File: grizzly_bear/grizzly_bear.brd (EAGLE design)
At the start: 76.2 x 41.3 mm, 59 parts, among them Q1 N-CHANNEL-MOSFET, Q2 N-CHANNEL-MOSFET, Q3 N-CHANNEL-MOSFET, Q4 N-CHANNEL-MOSFET, Q5 IPD90P03P4L, U1 A4940, U2 ATMEGA32U4-AU, U3 ACS714, U4 UA78L00, Y1 16MHz

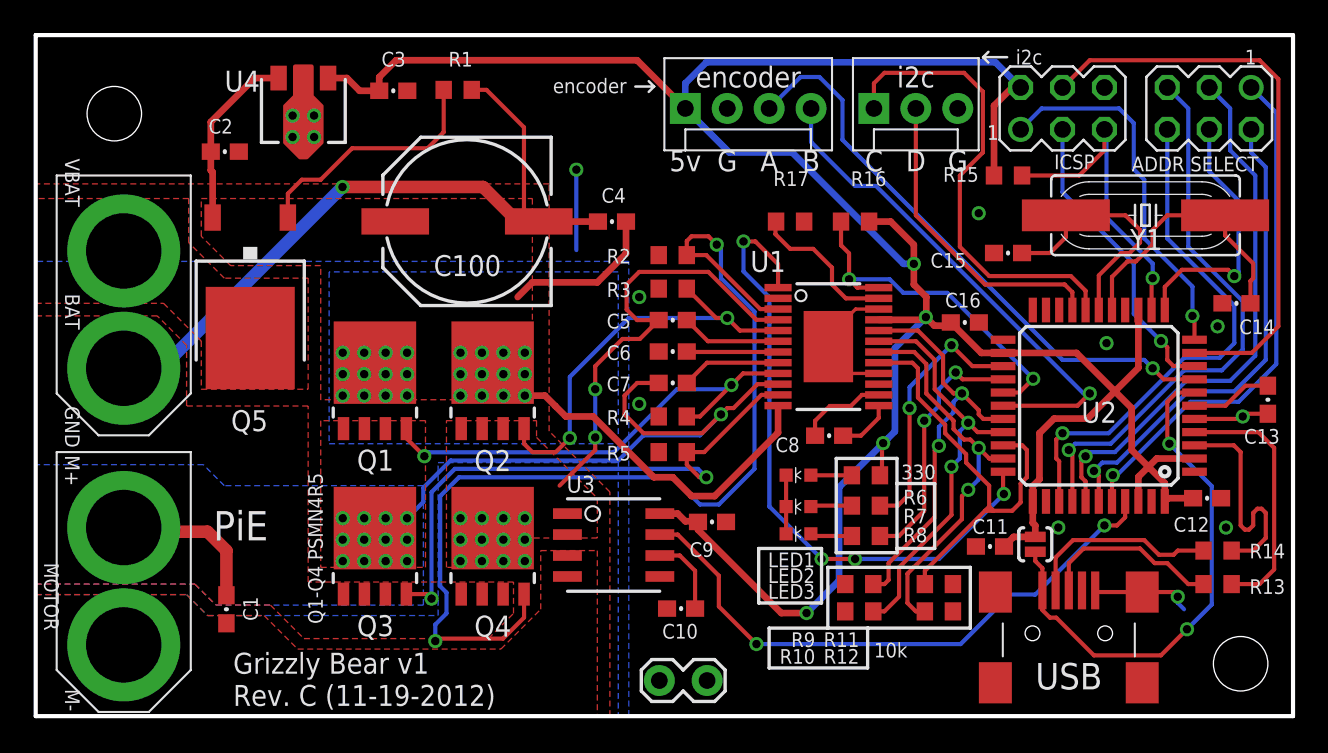
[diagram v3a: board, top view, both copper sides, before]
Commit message: Update Grizzly to Rev. D, mostly fixing grounds
Also fixes:
- Move XT60 connector back closer to edge
- Add GND symbol to pie.lbr
- Change LEDs to new 0805 footprint
- Adjust positions of 18pF caps
- Fix value of Ucap for USB (0.1uF-->1uF)
- Mounting holes on 1/4" grid (was 1/16")
- Use new MTA connector footprint

Change-Id: I2eb2c92b7e9216f9f3d609f47de082e2cb5dc4d4
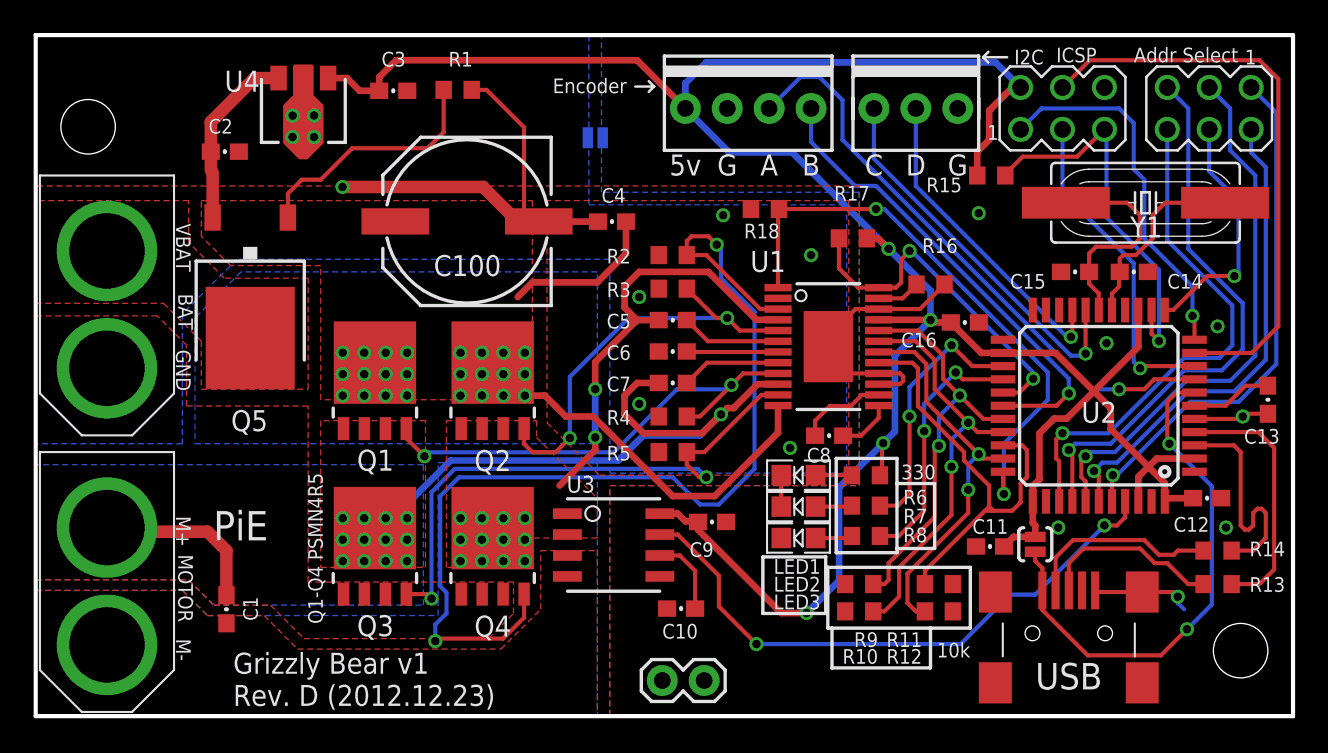
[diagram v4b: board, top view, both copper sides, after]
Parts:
- added R18: 10k, pie:R0603
- added SJ2: SOLDERJUMPERNO, pie:SJ_2S-NO
- C13: value 0.1uF -> 1uF
- JP1: device pie:1X02_LOCK -> pie:1X02
- JP3: device pie:MOLEX-1X4 -> pie:1X04-MTA
- JP4: device pie:MOLEX-1X3 -> pie:1X03-MTA
- LED1: value AMBR -> YEL; device pie:LED-0603 -> pie:LED-0805
- LED2, LED3: device pie:LED-0603 -> pie:LED-0805
- R16: value 10k -> 47k
- R17: value 47k -> 10k
- moved C14 6.51 mm to (66.5, 26.9), turned to 180 degrees
- moved R16 5.95 mm to (54.2, 26.2)
- moved C15 4.22 mm to (63.0, 26.9)
- moved R17 3.94 mm to (49.5, 29.0)
- moved JP3 3.81 mm to (43.2, 36.8)
- moved STANDOFF1 1.77 mm to (3.17, 35.7)
- moved U$18 1.02 mm to (0.25, 32.8)
- moved U$19 1.02 mm to (0.25, 16.0)
- moved R15 1.02 mm to (57.9, 32.8)
- moved STANDOFF2 0.79 mm to (73.0, 3.97)
- moved Y1 0.76 mm to (67.3, 31.1)
- moved LED3 0.25 mm to (46.2, 10.8), turned to 180 degrees
- turned LED1 to 180 degrees
- turned LED2 to 180 degrees
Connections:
- net 5V: now also R17.2; no longer R16.2
- net BATGND: now also C6.2, R16.2, R18.2, R2.2, R3.2, R4.2, R5.2, SJ2.1, U1.15, U1.16, U1.2, U1.22, U1.PAD
- net DRIVER-RESET: now also R18.1
- net FAULT: now also R17.1; no longer R16.1
- net GND: now also SJ2.2; no longer C6.2, R17.2, R2.2, R3.2, R4.2, R5.2, U1.15, U1.16, U1.2, U1.22, U1.PAD
- net RDEAD: now also R16.1; no longer R17.1
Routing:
- net GND: track 27.7 -> 19.0 mm, vias 14 -> 11
- net RDEAD: track 9.24 -> 2.64 mm
- net SCL: track 28.7 -> 23.5 mm, vias 0 -> 1
- net XTAL2: track 17.0 -> 11.9 mm
- net 5V: track 166.4 -> 161.6 mm
- net DRIVER-RESET: track 39.5 -> 35.0 mm, vias 4 -> 2
- net RESET: track 19.1 -> 23.5 mm
- net XTAL1: track 15.4 -> 13.3 mm
- net ENC2: track 30.8 -> 28.8 mm
- net SCK: track 18.4 -> 19.8 mm
- net DIP4: track 15.9 -> 14.8 mm
- net BATGND: track 44.5 -> 43.4 mm, vias 1 -> 6
- net SDA: track 19.0 -> 19.5 mm, vias 0 -> 1
- added copper zone on layer 16, net BATGND
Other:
- board text added: "Addr Select"
- board text added: "Encoder"
- board text added: "I2C"
- board text added: "Rev. D (2012.12.23)"
- board text removed: "ADDR SELECT"
- board text removed: "Rev. C (11-19-2012)"
- board text removed: "encoder"
- board text removed: "i2c"

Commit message: Updated Grizzly to Rev. E, mostly cleaning up sch
Change-Id: Ie27850869d7a5f893dd13d446602863972fe60ee
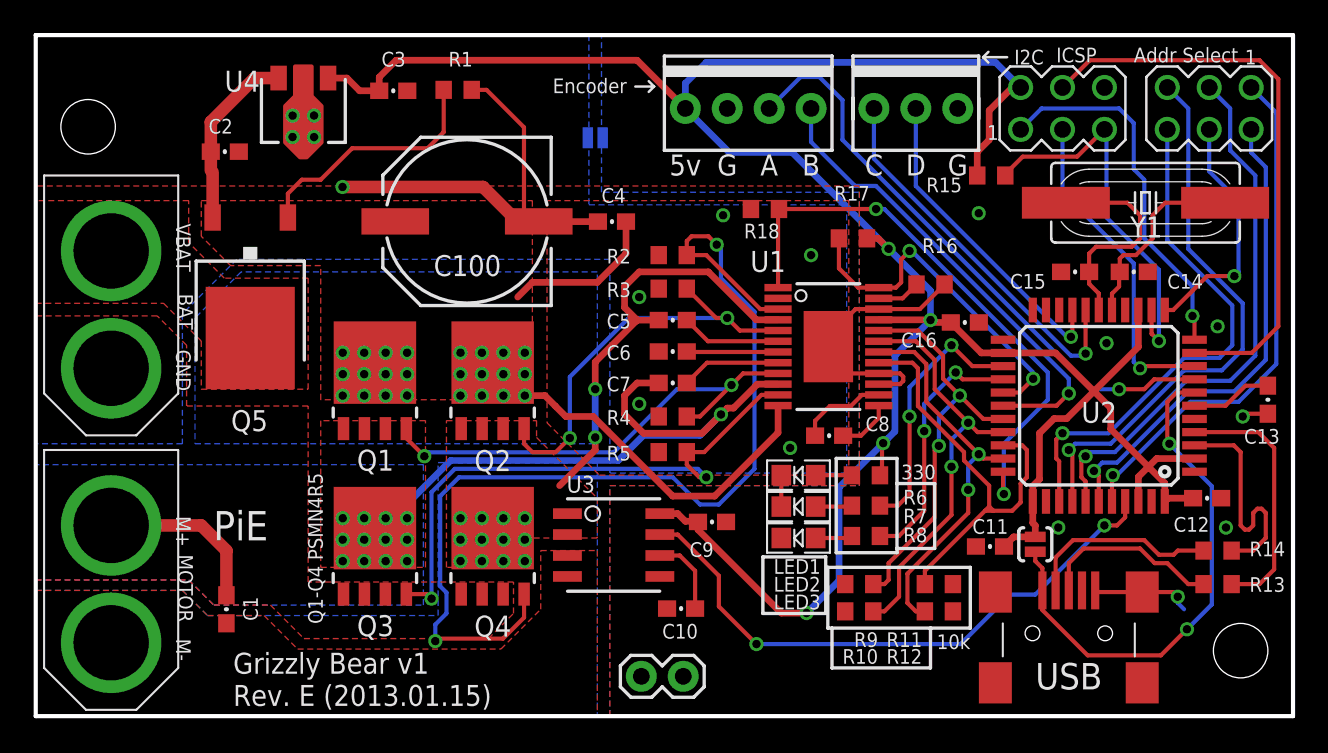
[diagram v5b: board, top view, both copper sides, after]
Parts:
- moved U$18 9.20 mm to (4.57, 24.6)
- moved U$19 9.09 mm to (4.57, 8.00)
- moved JP4 2.54 mm to (53.3, 36.8)
- moved JP1 0.25 mm to (38.0, 2.41)
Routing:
- net GND: track 19.0 -> 16.1 mm
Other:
- board text added: "Rev. E (2013.01.15)"
- board text removed: "Rev. D (2012.12.23)"

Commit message: Update silkscreen, copyright, paste on Grizzly
Change-Id: I853ac7017a0e5a7d6539925bc642fb125ce048da
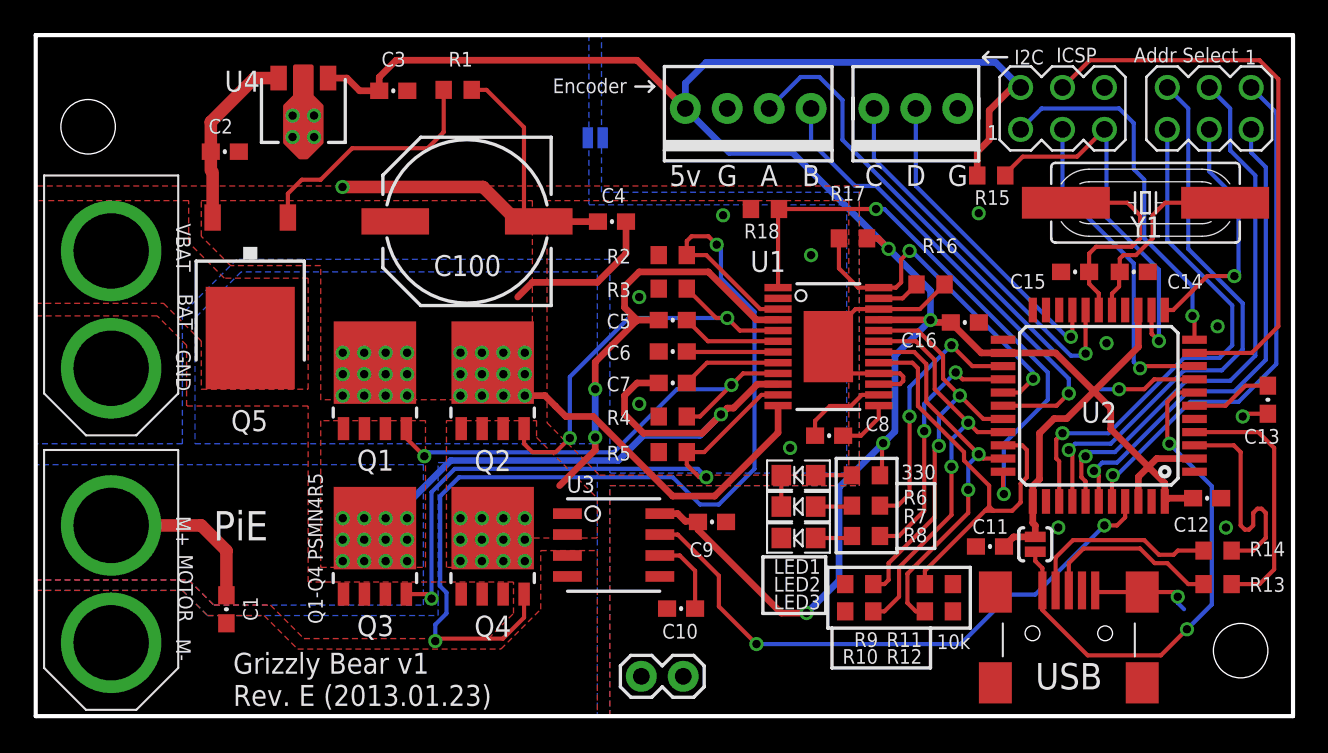
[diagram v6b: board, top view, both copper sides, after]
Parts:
- added U$1: (no value), pie:OSHW-LOGO-L
- turned JP3 to 180 degrees
- turned JP4 to 180 degrees
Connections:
- net 5V: now also JP3.4; no longer JP3.1
- net ENC1: now also JP3.2; no longer JP3.3
- net ENC2: now also JP3.1; no longer JP3.4
- net GND: now also JP3.3, JP4.1; no longer JP3.2, JP4.3
- net SCL: now also JP4.3; no longer JP4.1
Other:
- board text added: "Copyright (c) 2013, Pioneers in Engineering All rights reserved."
- board text added: "Design by: Jay Chenn, Keegan Mann, Robert Ou This design is open source hardware. For more information, visit pioneers.berkeley.edu/opensource"
- board text added: "Rev. E (2013.01.23)"
- board text removed: "Rev. E (2013.01.15)"

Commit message: rev F renamed to grizzly_bear 11/13
solder jumper replaced with large trace to connect ground planes,
copyright info stop mask conflicts resolved
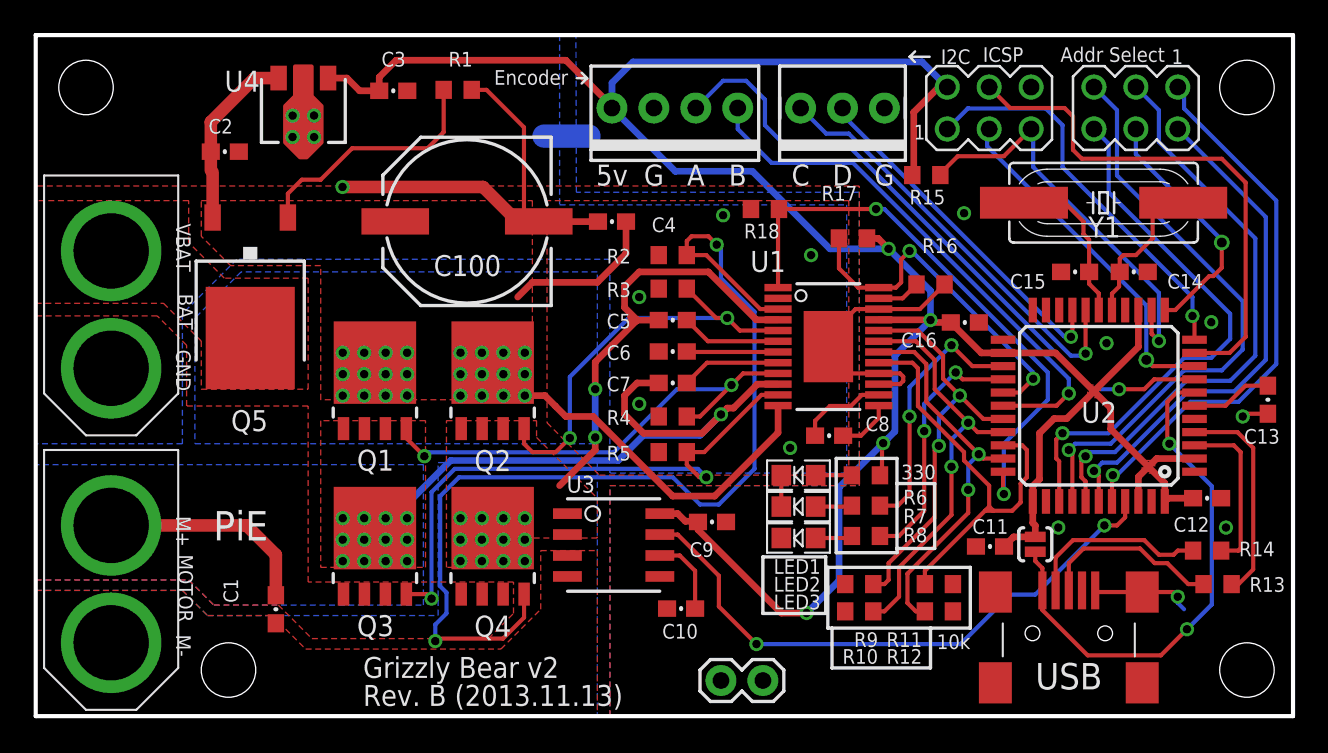
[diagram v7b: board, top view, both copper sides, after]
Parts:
- removed SJ2: SOLDERJUMPERNO, pie:SJ_2S-NO
- added STANDOFF3, STANDOFF4: STAND-OFF, pie:STAND-OFF
- moved JP1 4.83 mm to (42.8, 2.16), turned to 180 degrees
- moved SV1 4.45 mm to (66.7, 36.9)
- moved JP3 4.45 mm to (38.7, 36.9)
- moved JP4 4.45 mm to (48.9, 36.9)
- moved JP6 4.45 mm to (57.8, 36.9)
- moved R15 3.94 mm to (54.0, 32.8)
- moved C1 3.00 mm to (14.6, 6.48)
- moved Y1 2.54 mm to (64.7, 31.1)
- moved STANDOFF1 2.38 mm to (3.05, 38.1)
- moved STANDOFF2 1.23 mm to (73.4, 2.79)
- moved R14 0.64 mm to (71.0, 10.0)
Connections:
- removed net GND: C10.1, C11.1, C12.2, C13.2, C14.1, C15.1, C16.2, C2.2, C3.2, C9.2, JP1.1, JP1.2, JP3.3, JP4.1, JP6.6, LED1.C, LED2.C, LED3.C, R10.2, R11.2, R12.2, R9.2, SJ2.2, U$2.G, U$2.S1, U$2.S2, U$2.S3, U$2.S4, U2.15, U2.23, U2.35, U2.43, U2.5, U3.5, U4.COMMON
- net BATGND: now also C10.1, C11.1, C12.2, C13.2, C14.1, C15.1, C16.2, C2.2, C3.2, C9.2, JP1.1, JP1.2, JP3.3, JP4.1, JP6.6, LED1.C, LED2.C, LED3.C, R10.2, R11.2, R12.2, R9.2, U$2.G, U$2.S1, U$2.S2, U$2.S3, U$2.S4, U2.15, U2.23, U2.35, U2.43, U2.5, U3.5, U4.COMMON; no longer SJ2.1
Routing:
- net BATGND: track 43.4 -> 62.3 mm, vias 6 -> 17
- net GND: track 16.1 -> 0.00 mm, vias 11 -> 0
- net ENC2: track 28.8 -> 32.8 mm
- net D-: track 14.0 -> 10.0 mm
- net ENC1: track 36.1 -> 39.8 mm
- net XTAL1: track 13.3 -> 9.82 mm
- net MOSI: track 35.0 -> 32.0 mm
- net SCL: track 23.5 -> 26.2 mm
- net M+: track 46.3 -> 48.8 mm
- net XTAL2: track 11.9 -> 9.38 mm
- net D+: track 15.5 -> 13.0 mm
- net SDA: track 19.5 -> 21.5 mm
- net DIP3: track 33.2 -> 35.0 mm
- net MISO: track 22.4 -> 24.3 mm
- net DIP5: track 34.0 -> 35.9 mm
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- added copper zone on layer 1, net 5V
- removed copper zone on layer 1, net GND
- removed copper zone on layer 16, net GND
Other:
- board text added: "Design by: Jay Chenn, Keegan Mann, Robert Ou, Jeffrey Jacinto This design is open source hardware. For more information, visit pioneers.berkeley.edu/opensource"
- board text added: "Grizzly Bear v2"
- board text added: "Rev. B (2013.11.13)"
- board text removed: "Design by: Jay Chenn, Keegan Mann, Robert Ou This design is open source hardware. For more information, visit pioneers.berkeley.edu/opensource"
- board text removed: "Grizzly Bear v1"
- board text removed: "Rev. E (2013.01.23)"

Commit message: Enclosure Issues Resolved
Address Select component moved, Resistor 15 moved, I2C and encoder pins
moved (is the resulting placement of "C" "D" and "G" fine?), crystal
moved, Resistor 9,10,11,12 test vias aligned
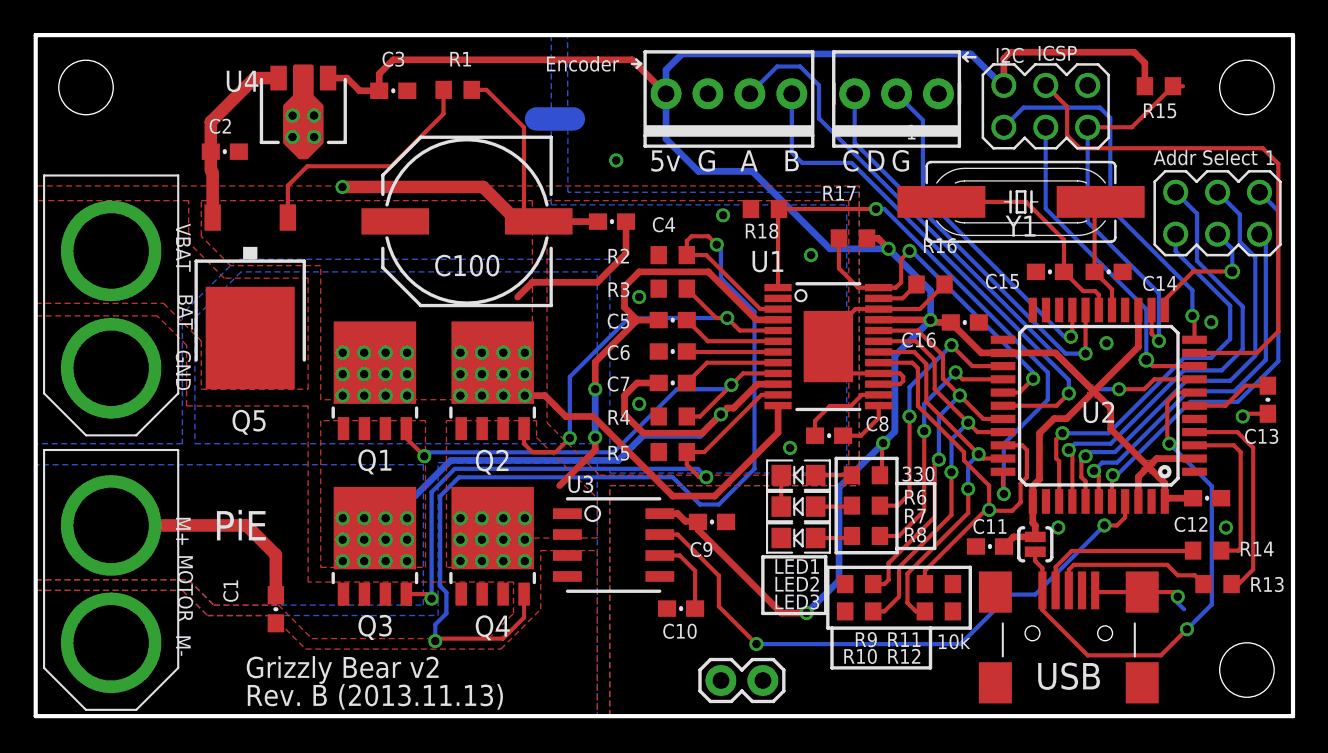
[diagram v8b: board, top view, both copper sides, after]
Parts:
- removed STANDOFF4: STAND-OFF, pie:STAND-OFF
- C11: value 0.1uF -> 0.1 uF
- moved R15 15.1 mm to (68.1, 38.2)
- moved SV1 8.07 mm to (71.6, 30.5)
- moved Y1 5.00 mm to (59.7, 31.2)
- moved JP6 3.43 mm to (61.2, 37.0)
- moved JP3 3.39 mm to (42.0, 37.7)
- moved JP4 3.39 mm to (52.2, 37.7)
- moved C14 1.52 mm to (65.0, 26.9)
- moved C15 1.52 mm to (61.5, 26.9)
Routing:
- net DIP3: track 35.0 -> 26.6 mm
- net DIP2: track 31.4 -> 22.9 mm
- net DIP5: track 35.9 -> 27.5 mm
- net DIP6: track 33.0 -> 24.6 mm
- net DIP1: track 33.6 -> 25.2 mm
- net 5V: track 161.5 -> 168.7 mm
- net DIP4: track 15.1 -> 8.04 mm
- net XTAL1: track 9.82 -> 13.9 mm
- net ENC1: track 39.8 -> 37.2 mm
- net XTAL2: track 9.38 -> 7.14 mm
- net ENC2: track 32.8 -> 31.2 mm
- net MISO: track 24.3 -> 22.8 mm
- net SCK: track 21.1 -> 19.7 mm
- net SCL: track 26.2 -> 24.9 mm
- net RESET: track 24.8 -> 23.6 mm
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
